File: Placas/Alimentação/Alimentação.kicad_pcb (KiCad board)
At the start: 2 copper layers, 73.2 x 80.7 mm, 57 parts, among them J1 Conn_02x02_ZigZag, J10 Conn_01x01_Pin, J11 Conn_01x01_Pin, J12 Conn_01x01_Pin, J13 Conn_01x01_Pin, J14 Conn_01x01_Pin, J15 Conn_01x01_Pin, J16 Conn_01x01_Pin, J17 Conn_01x01_Pin, J2 Conn_02x03_ZigZag, J3 Conn_02x02_ZigZag, J4 Conn_02x01, J5 Conn_01x01_Pin, J6 Conn_01x01_Pin, J7 Conn_01x01_Pin, J8 Conn_01x01_Pin, J9 Conn_01x01_Pin, U1 YAAJ_DCDC_StepDown_LM2596, U2 Módulo XL6009, U3 XL6009, U4 XL6009, U5 XL6009

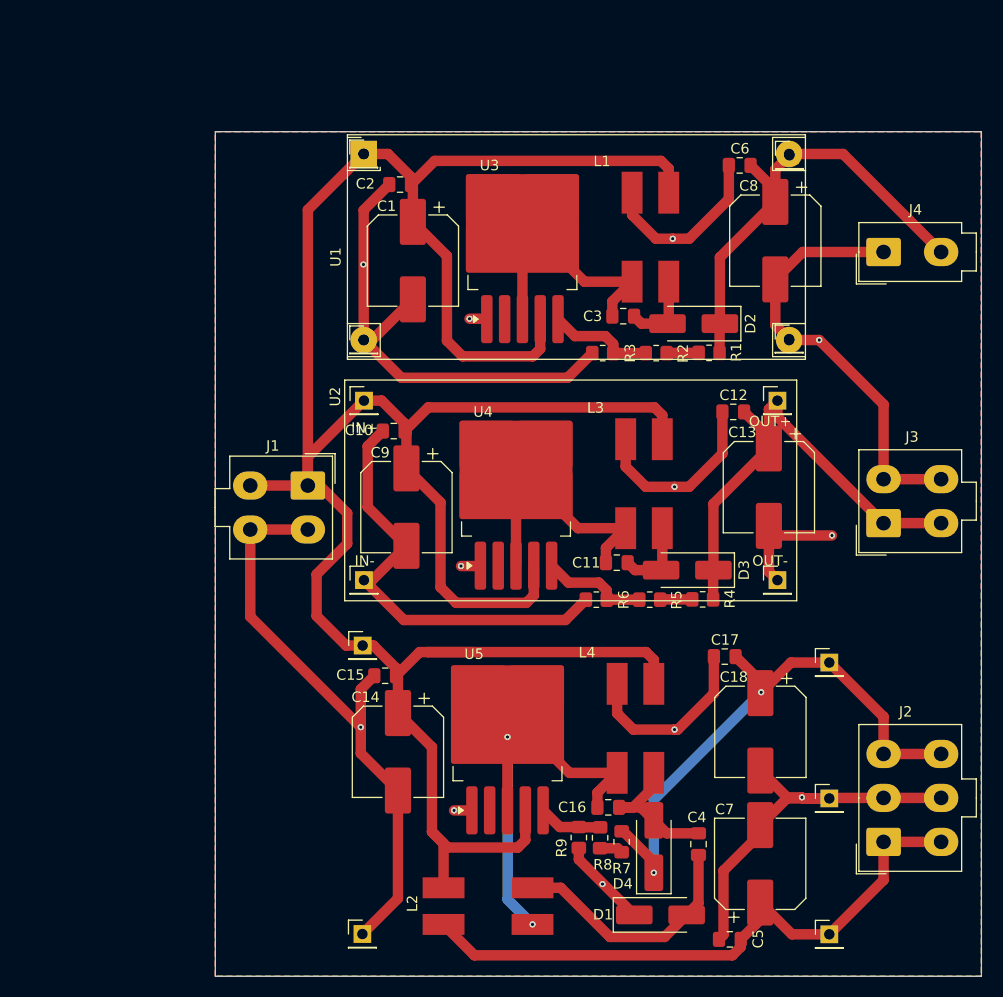
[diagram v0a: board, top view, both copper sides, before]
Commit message: Adição de circuitos opcionais para PWM
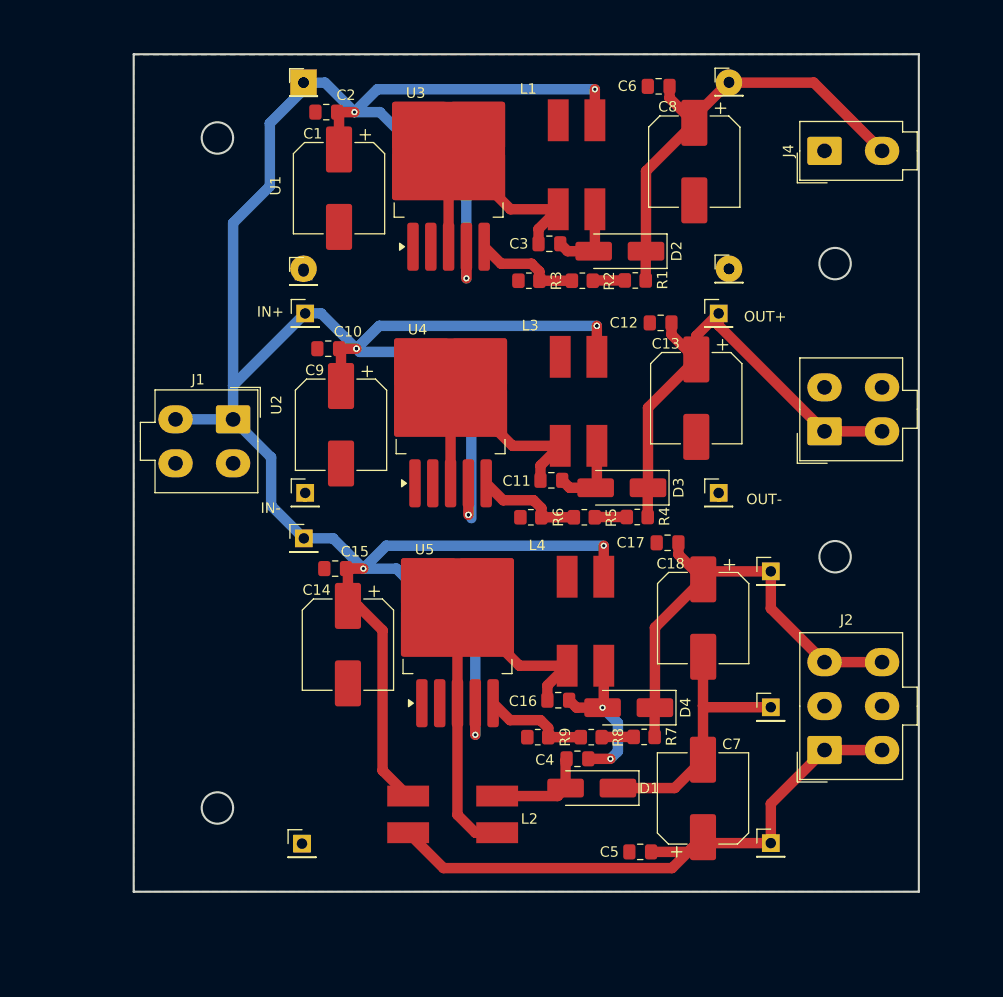
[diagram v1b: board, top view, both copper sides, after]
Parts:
- moved C4 14.1 mm to (97.4, 108.2), turned to 180 degrees
- moved D1 13.8 mm to (98.7, 111.0), turned to 180 degrees
- moved D4 13.5 mm to (102.3, 103.3), turned to 180 degrees
- moved C18 12.2 mm to (109.4, 94.8)
- moved C17 12.2 mm to (106.0, 87.6)
- moved C5 12.0 mm to (103.4, 117.1)
- moved J13 11.7 mm to (71.2, 87.1)
- moved C14 11.3 mm to (75.5, 97.3)
- moved C15 11.3 mm to (74.2, 90.0)
- moved C16 11.3 mm to (95.5, 102.6)
- moved L4 11.3 mm to (95.4, 101.3)
- moved U5 11.3 mm to (85.9, 95.2)
- moved J4 11.2 mm to (121.0, 50.1)
- moved C12 11.0 mm to (105.3, 66.6)
- moved C13 11.0 mm to (108.7, 73.8)
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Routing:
- net GND: track 303.3 -> 25.6 mm, vias 12 -> 0
- net Net-(D1-A): track 23.7 -> 9.69 mm
- net +15V_sym: track 55.4 -> 44.5 mm, vias 2 -> 0
- net +12V: track 269.3 -> 276.4 mm, vias 0 -> 12
- net Net-(U5-FB): track 6.12 -> 10.2 mm
- net /Conversor 12 to 15V - Simétrico/SEPIC_XL6010/SW: track 41.1 -> 37.4 mm, vias 2 -> 0
- net /Conversor 12 to 15V - Simétrico/SEPIC_XL6010/L_out: track 14.1 -> 15.4 mm, vias 0 -> 2
- net Net-(R7-Pad2): track 2.24 -> 3.07 mm
- added copper zone on F.Cu, net GND
- removed copper zone on F.Cu, net +12V
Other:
- board size 73.2 x 80.7 mm -> 75 x 80 mm

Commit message: Modificações nas duas placas, adição de furos para montagem, melhora na posição dos micros e conectores para comunicação SPI
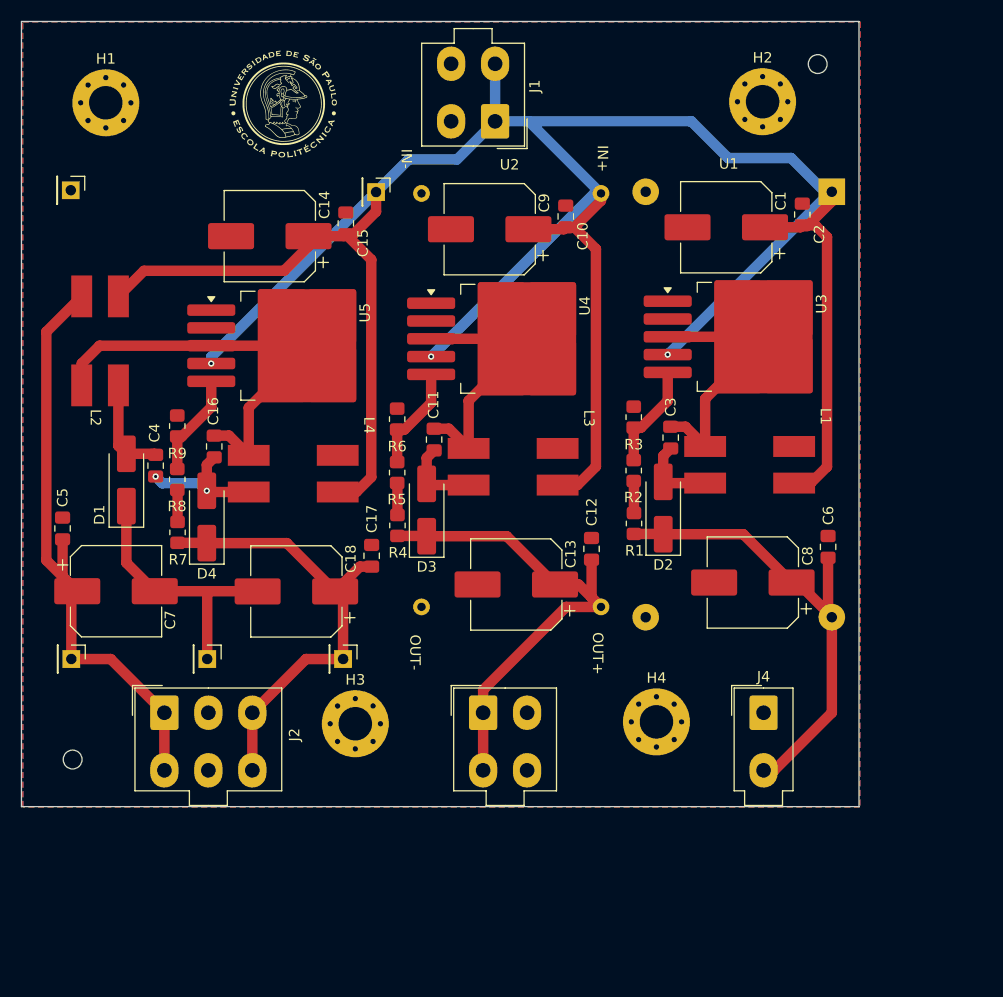
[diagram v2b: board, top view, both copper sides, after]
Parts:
- removed J10, J11, J12, J5, J6, J7, J8, J9: Conn_01x01_Pin, Connector_PinHeader_2.54mm:PinHeader_1x01_P2.54mm_Vertical
- added G***: LOGO, Logos:logo_poli_13mm, F.Cu at (69.3, 45.6)
- added H1: MountingHole_Pad, MountingHole:MountingHole_3.2mm_M3_Pad_Via, F.Cu at (52.3, 45.5)
- added H2: MountingHole_Pad, MountingHole:MountingHole_3.2mm_M3_Pad_Via, F.Cu at (115.1, 45.4)
- added H3: MountingHole_Pad, MountingHole:MountingHole_3.2mm_M3_Pad_Via, F.Cu at (76.2, 104.9)
- added H4: MountingHole_Pad, MountingHole:MountingHole_3.2mm_M3_Pad_Via, F.Cu at (104.9, 104.7)
- moved J15 69.1 mm to (49.0, 98.7), turned to -90 degrees
- moved J14 66.2 mm to (49.0, 53.9), turned to -90 degrees
- moved C5 63.2 mm to (48.2, 86.2), turned to 90 degrees
- moved J2 63.2 mm to (57.9, 103.8), turned to 0 degrees
- moved L2 59.7 mm to (49.0, 74.5), turned to 0 degrees
- moved C7 59.5 mm to (53.3, 92.2), turned to 0 degrees
- moved J16 54.0 mm to (62.0, 98.7), turned to -90 degrees
- moved J4 54.0 mm to (115.2, 103.8), turned to 0 degrees
- moved D1 53.3 mm to (54.3, 81.6), turned to 90 degrees
- moved U1 51.5 mm to (121.7, 54.0), turned to -90 degrees
- moved C4 49.1 mm to (57.1, 80.2), turned to 90 degrees
- moved R7 48.7 mm to (59.2, 86.6), turned to 90 degrees
- moved C6 46.9 mm to (121.3, 88.0), turned to 90 degrees
- moved R8 46.6 mm to (59.2, 81.5), turned to 90 degrees
- moved C2 46.5 mm to (118.9, 56.2), turned to 90 degrees
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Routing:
- net +12V: track 276.4 -> 264.2 mm, vias 12 -> 3
- net /Conversor 12 to 15V - Simétrico/SEPIC_XL6010/L_out: track 15.4 -> 13.0 mm
- net 5V: track 44.0 -> 46.0 mm
- net 15V: track 47.7 -> 49.4 mm
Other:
- board size 75 x 80 mm -> 80 x 75 mm

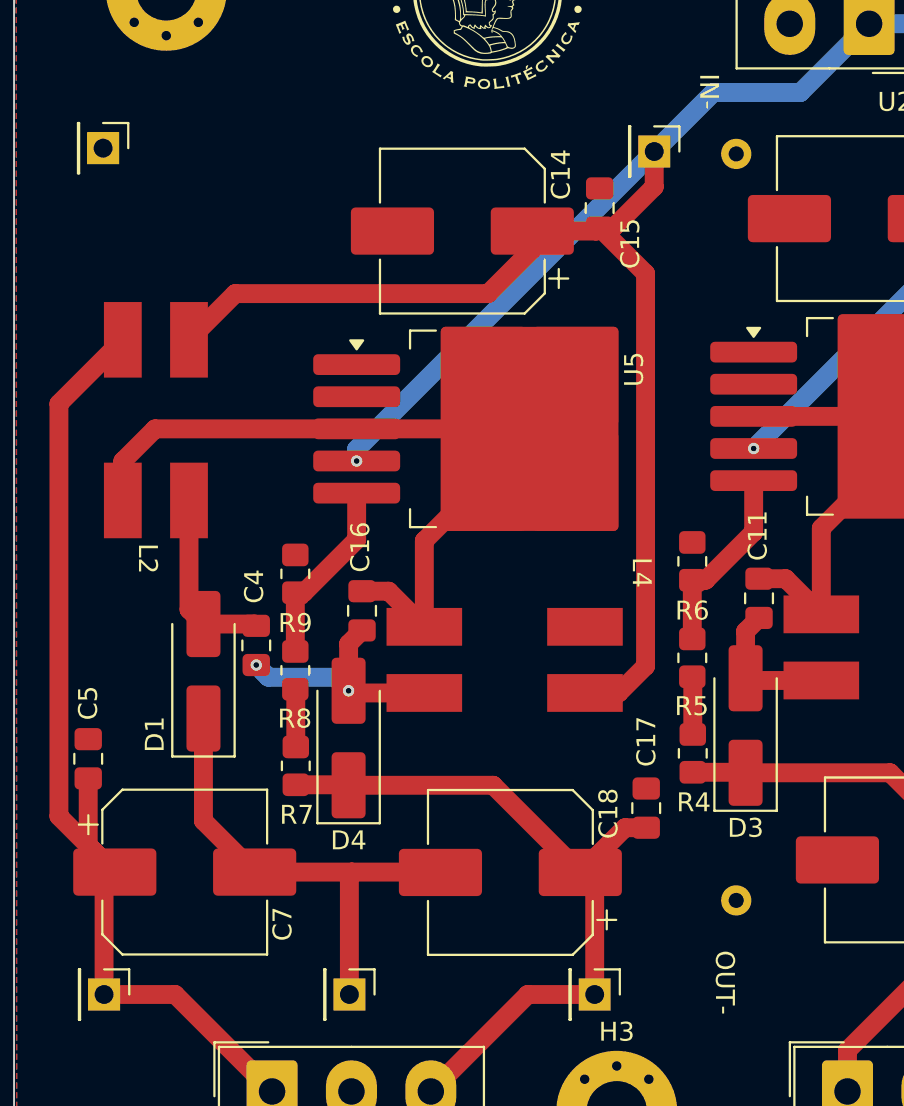
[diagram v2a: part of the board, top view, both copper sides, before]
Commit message: Criação dos arquivos em C para o firmware dos dois micros e script em python para salvar aquisição dos dados e envio de comandos
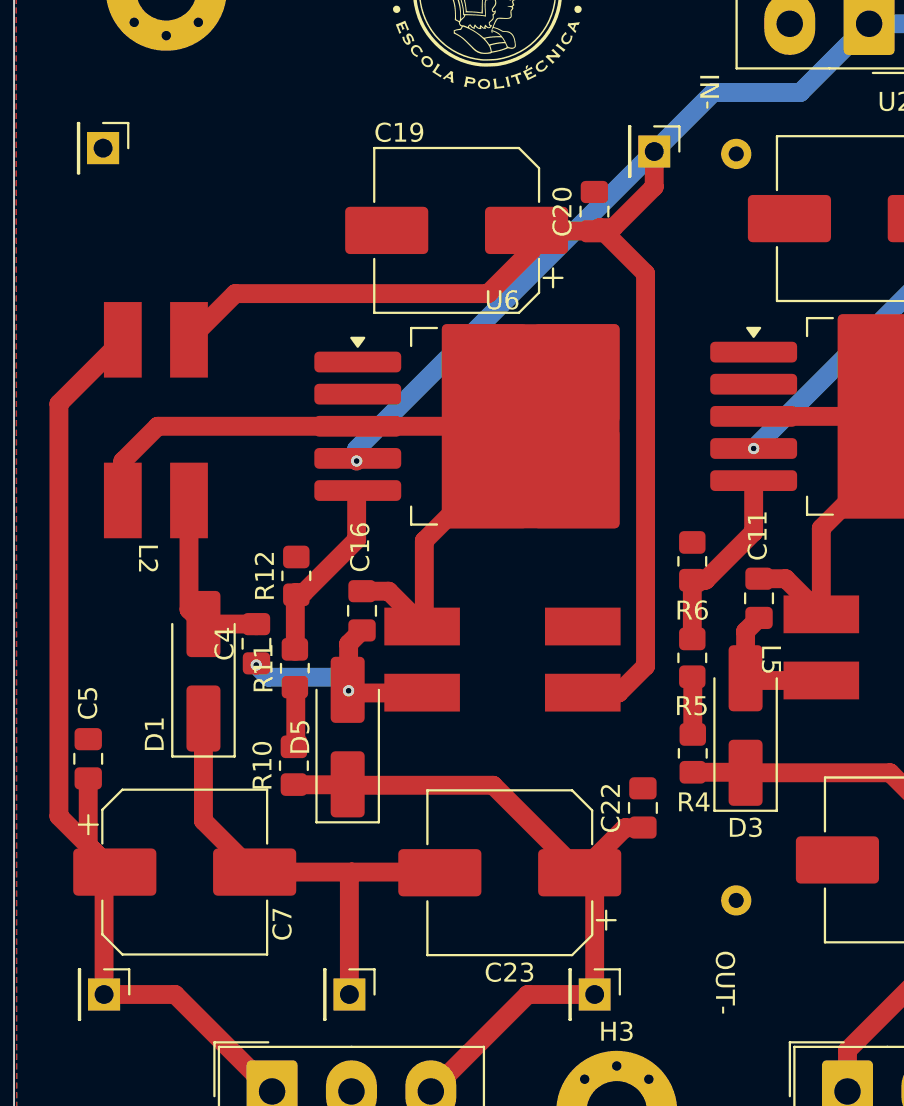
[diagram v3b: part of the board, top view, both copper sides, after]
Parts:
- removed C14, C18: 220u, Capacitor_SMD:CP_Elec_8x10.5
- removed C15, C17: 1u, Capacitor_SMD:C_0805_2012Metric_Pad1.18x1.45mm_HandSolder
- removed D4: SS14, Diode_SMD:D_SMA_Handsoldering
- removed L4: MSD1260t, Coupled_inductors:Msd1260t
- removed R7: 10k, Resistor_SMD:R_0805_2012Metric_Pad1.20x1.40mm_HandSolder
- removed R8, R9: 1k, Resistor_SMD:R_0805_2012Metric_Pad1.20x1.40mm_HandSolder
- removed U5: XL6009, Package_TO_SOT_SMD:TO-263-5_TabPin3
- added C19: 220u, Capacitor_SMD:CP_Elec_8x10.5, F.Cu at (67.7, 58.2)
- added C20: 1u, Capacitor_SMD:C_0805_2012Metric_Pad1.18x1.45mm_HandSolder, F.Cu at (75.0, 57.2)
- added C22: 1u, Capacitor_SMD:C_0805_2012Metric_Pad1.18x1.45mm_HandSolder, F.Cu at (77.5, 88.8)
- added C23: 220u, Capacitor_SMD:CP_Elec_8x10.5, F.Cu at (70.5, 92.2)
- added D5: SS14, Diode_SMD:D_SMA_Handsoldering, F.Cu at (61.9, 85.0)
- added L5: MSD1260t, Coupled_inductors:Msd1260t, F.Cu at (63.9, 78.2)
- added R10: 10k, Resistor_SMD:R_0805_2012Metric_Pad1.20x1.40mm_HandSolder, F.Cu at (59.1, 86.6)
- added R11: 1k, Resistor_SMD:R_0805_2012Metric_Pad1.20x1.40mm_HandSolder, F.Cu at (59.1, 81.4)
- added R12: 1k, Resistor_SMD:R_0805_2012Metric_Pad1.20x1.40mm_HandSolder, F.Cu at (59.2, 76.5)
- added U6: XL6009, Package_TO_SOT_SMD:TO-263-5_TabPin3, F.Cu at (70.1, 68.6)
- moved C4 0.09 mm to (57.1, 80.1)
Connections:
- C4 pad 1: /Conversor 12 to 15V - Simétrico/SEPIC_XL6010/L_out -> /Conversor 12 to 15V - Simétrico/L_out
- L2 pad 3: /Conversor 12 to 15V - Simétrico/SEPIC_XL6010/SW -> /Conversor 12 to 15V - Simétrico/SW
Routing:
- net /Conversor 12 to 15V - Simétrico/SW: track 0.00 -> 24.4 mm
- net /Conversor 12 to 15V - Simétrico/SEPIC_XL6010/SW: track 37.4 -> 13.1 mm
- net Net-(U6-FB): track 0.00 -> 9.98 mm
- net Net-(U5-FB): track 9.98 -> 0.00 mm
- net Net-(R7-Pad2): track 3.07 -> 0.00 mm
- net Net-(R10-Pad2): track 0.00 -> 3.07 mm
